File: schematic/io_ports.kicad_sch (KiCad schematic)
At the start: 5 parts, among them J1 Cartridge Port, J2 Expansion Port

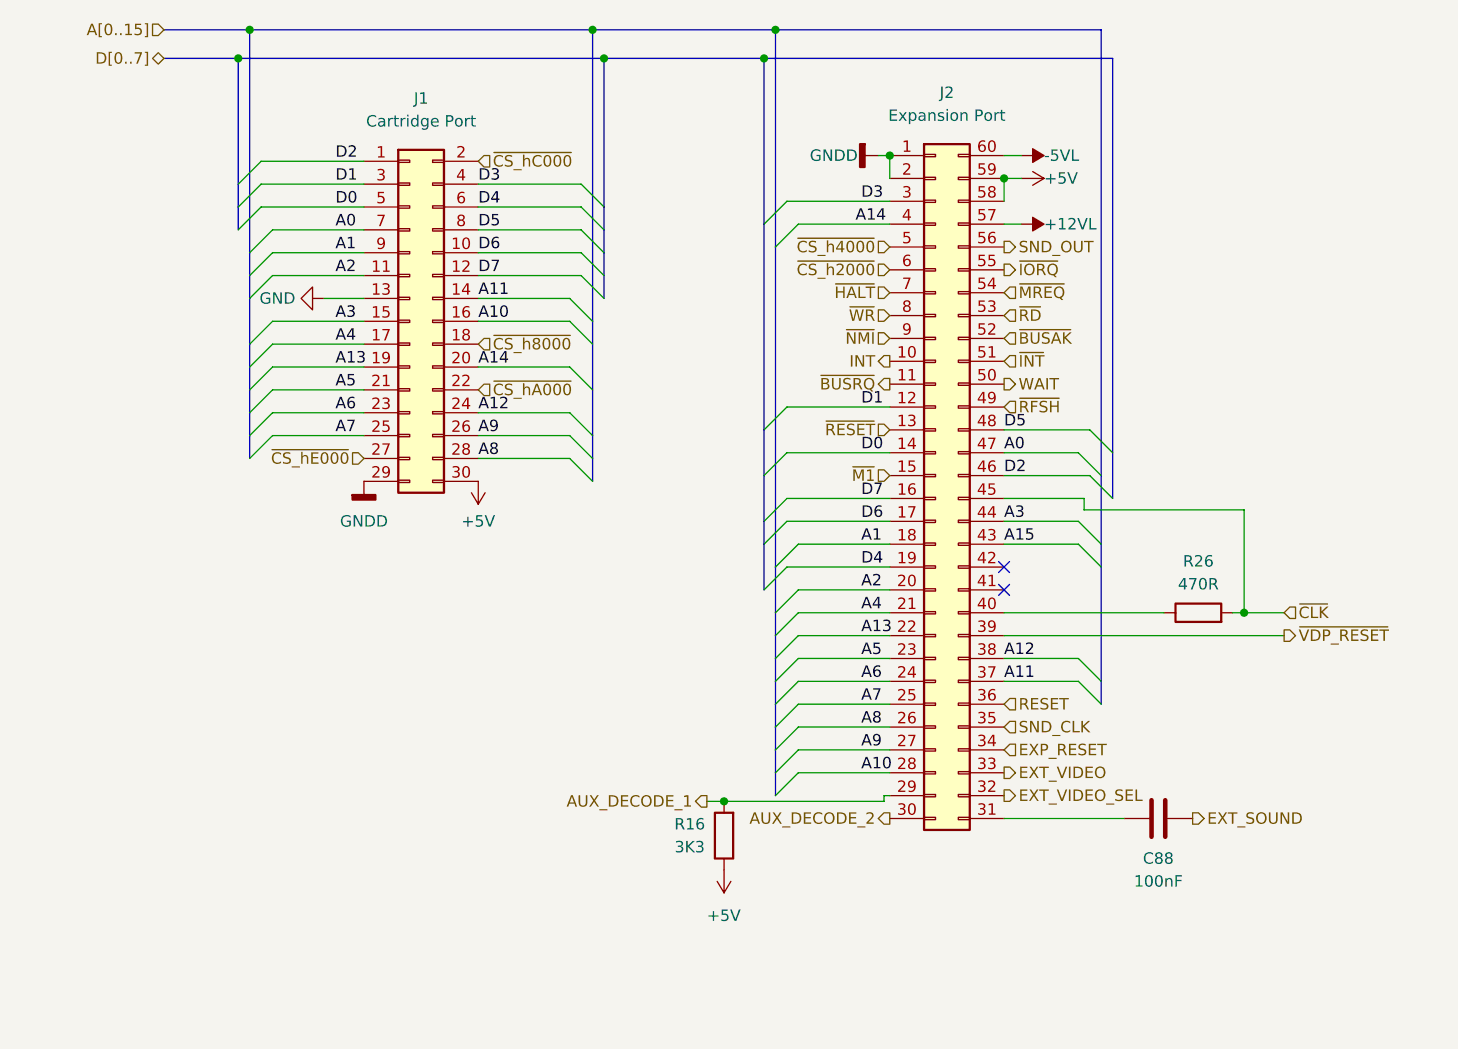
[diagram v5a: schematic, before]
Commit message: adjusted size of the sheets. added pcb version to the rev field. F.0... the 0 is for future fixes on my end. RF PCB is E.0.
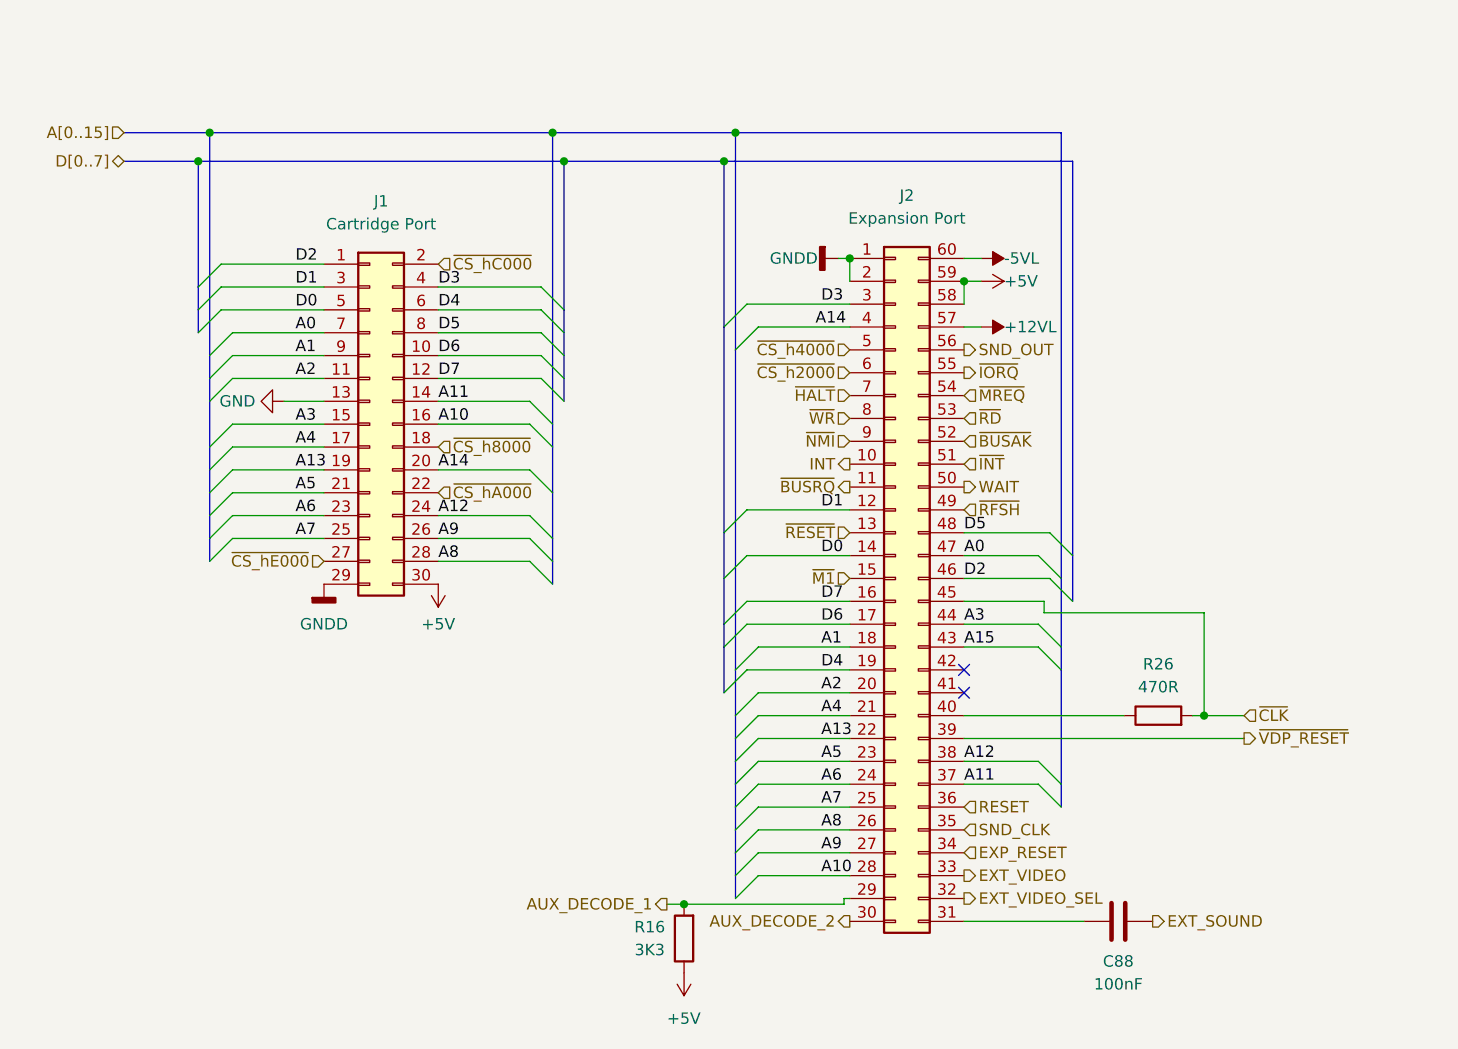
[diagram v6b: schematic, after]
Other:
- title: (none) -> Colecovision Schematic
- moved on the sheet: C88, J1, J2, R16, R26

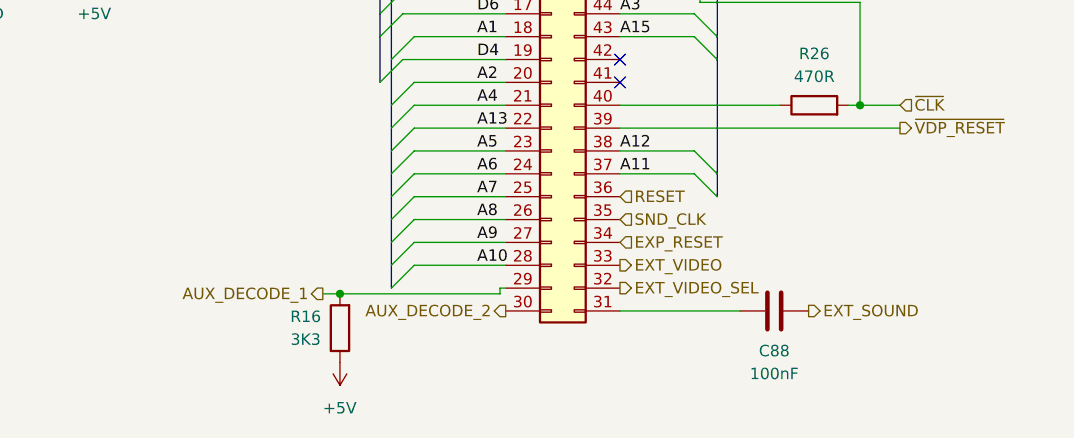
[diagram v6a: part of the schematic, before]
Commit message: cleanup, and started associating components
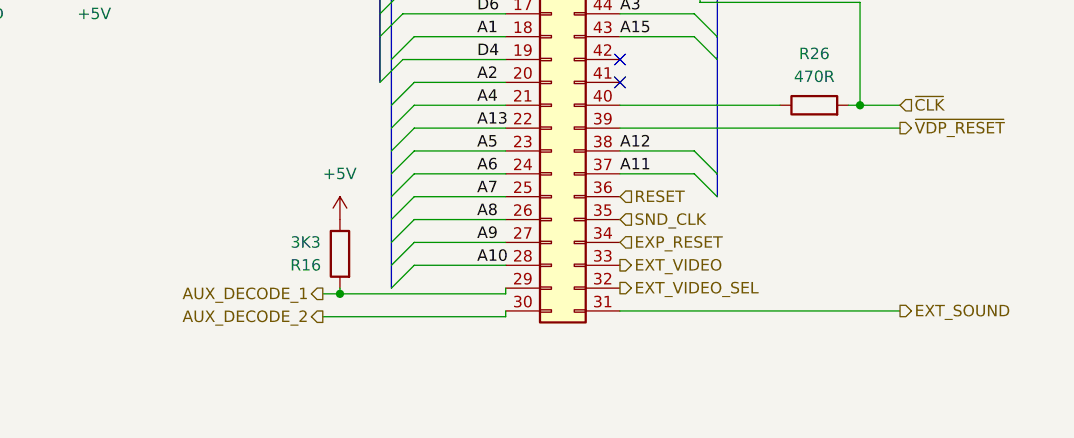
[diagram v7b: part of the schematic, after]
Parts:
- removed C88: 100nF, symbol Device:C
- R16, R26: footprint (none) -> Resistor_THT:R_Axial_DIN0207_L6.3mm_D2.5mm_P7.62mm_Horizontal
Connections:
- net EXT_SOUND: now also J2.31 (Pin_31)
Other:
- moved on the sheet: R16
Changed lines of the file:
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@@
+    (stroke (width 0) (type default) (color 0 0 0 0))
+  )
+  (wire (pts (xy 158.75 129.54) (xy 158.75 130.175))
     (stroke (width 0) (type default) (color 0 0 0 0))
   )
@@
     (stroke (width 0) (type default) (color 0 0 0 0))
   )
-  (wire (pts (xy 158.115 129.54) (xy 158.115 130.175))
-    (stroke (width 0) (type default) (color 0 0 0 0))
-  )
   (bus (pts (xy 125.73 44.45) (xy 125.73 76.835))
     (stroke (width 0) (type default) (color 0 0 0 0))
@@
     (stroke (width 0) (type default) (color 0 0 0 0))
   )
+  (wire (pts (xy 138.43 132.715) (xy 158.75 132.715))
+    (stroke (width 0) (type default) (color 0 0 0 0))
+  )
   (bus (pts (xy 144.78 101.6) (xy 144.78 106.68))
     (stroke (width 0) (type default) (color 0 0 0 0))
@@
     (stroke (width 0) (type default) (color 0 0 0 0))
   )
-  (wire (pts (xy 158.75 129.54) (xy 158.115 129.54))
-    (stroke (width 0) (type default) (color 0 0 0 0))
-  )
   (wire (pts (xy 171.45 109.22) (xy 189.23 109.22))
     (stroke (width 0) (type default) (color 0 0 0 0))
@@
     (stroke (width 0) (type default) (color 0 0 0 0))
   )
+  (wire (pts (xy 140.335 129.54) (xy 140.335 130.175))
+    (stroke (width 0) (type default) (color 0 0 0 0))
+  )
   (wire (pts (xy 180.34 97.79) (xy 198.12 97.79))
     (stroke (width 0) (type default) (color 0 0 0 0))
@@
     (stroke (width 0) (type default) (color 0 0 0 0))
   )
-  (wire (pts (xy 140.335 130.175) (xy 158.115 130.175))
+  (wire (pts (xy 140.335 130.175) (xy 158.75 130.175))
     (stroke (width 0) (type default) (color 0 0 0 0))
   )
@@
     (stroke (width 0) (type default) (color 0 0 0 0))
   )
-  (wire (pts (xy 171.45 132.08) (xy 184.785 132.08))
+  (wire (pts (xy 171.45 132.08) (xy 202.565 132.08))
     (stroke (width 0) (type default) (color 0 0 0 0))
   )
@@
     (stroke (width 0) (type default) (color 0 0 0 0))
   )
+  (wire (pts (xy 158.75 132.715) (xy 158.75 132.08))
+    (stroke (width 0) (type default) (color 0 0 0 0))
+  )
   (bus (pts (xy 127 69.215) (xy 127 71.755))
     (stroke (width 0) (type default) (color 0 0 0 0))
@@
     (effects (font (size 1.27 1.27)) (justify left bottom))
   )
-  (hierarchical_label "AUX_DECODE_2" (shape output) (at 158.75 132.08 180)
+  (hierarchical_label "AUX_DECODE_2" (shape output) (at 138.43 132.715 180)
     (effects (font (size 1.27 1.27)) (justify right))
   )
@@
     (effects (font (size 1.27 1.27)) (justify right))
   )
-  (hierarchical_label "EXT_SOUND" (shape output) (at 192.405 132.08 0)
+  (hierarchical_label "EXT_SOUND" (shape output) (at 202.565 132.08 0)
     (effects (font (size 1.27 1.27)) (justify left))
   )
@@
     (pin "9")
   )
-  (symbol (lib_id "power:+5V") (at 140.335 137.795 180) (unit 1)
+  (symbol (lib_id "power:+5V") (at 140.335 121.92 0) (mirror y) (unit 1)
     (in_bom yes) (on_board yes)
-    (property "Reference" "#PWR?" (id 0) (at 140.335 133.985 0)
-      (effects (font (size 1.27 1.27)) hide)
-    )
-    (property "Value" "+5V" (id 1) (at 138.43 142.875 0)
+    (property "Reference" "#PWR0201" (id 0) (at 140.335 125.73 0)
+      (effects (font (size 1.27 1.27)) hide)
+    )
+    (property "Value" "+5V" (id 1) (at 138.43 116.84 0)
       (effects (font (size 1.27 1.27)) (justify right))
     )
-    (property "Footprint" "" (id 2) (at 140.335 137.795 0)
-      (effects (font (size 1.27 1.27)) hide)
-    )
-    (property "Datasheet" "" (id 3) (at 140.335 137.795 0)
+    (property "Footprint" "" (id 2) (at 140.335 121.92 0)
+      (effects (font (size 1.27 1.27)) hide)
+    )
+    (property "Datasheet" "" (id 3) (at 140.335 121.92 0)
       (effects (font (size 1.27 1.27)) hide)
     )
@@
     (property "Reference" "R26" (id 0) (at 193.04 103.505 90))
     (property "Value" "470R" (id 1) (at 193.04 106.045 90))
-    (property "Footprint" "" (id 2) (at 193.04 110.998 90)
+    (property "Footprint" "Resistor_THT:R_Axial_DIN0207_L6.3mm_D2.5mm_P7.62mm_Horizontal" (id 2) (at 193.04 110.998 90)
       (effects (font (size 1.27 1.27)) hide)
     )
@@
   (symbol (lib_id "power:+5V") (at 173.355 60.96 270) (unit 1)
     (in_bom yes) (on_board yes)
-    (property "Reference" "#PWR?" (id 0) (at 169.545 60.96 0)
+    (property "Reference" "#PWR0204" (id 0) (at 169.545 60.96 0)
       (effects (font (size 1.27 1.27)) hide)
     )
@@
     (pin "9")
   )
-  (symbol (lib_id "Device:R") (at 140.335 133.985 180) (unit 1)
+  (symbol (lib_id "Device:R") (at 140.335 125.73 0) (mirror y) (unit 1)
     (in_bom yes) (on_board yes)
-    (property "Reference" "R16" (id 0) (at 136.525 132.715 0))
-    (property "Value" "3K3" (id 1) (at 136.525 135.255 0))
-    (property "Footprint" "" (id 2) (at 142.113 133.985 90)
-      (effects (font (size 1.27 1.27)) hide)
-    )
-    (property "Datasheet" "~" (id 3) (at 140.335 133.985 0)
+    (property "Reference" "R16" (id 0) (at 136.525 127 0))
+    (property "Value" "3K3" (id 1) (at 136.525 124.46 0))
+    (property "Footprint" "Resistor_THT:R_Axial_DIN0207_L6.3mm_D2.5mm_P7.62mm_Horizontal" (id 2) (at 142.113 125.73 90)
+      (effects (font (size 1.27 1.27)) hide)
+    )
+    (property "Datasheet" "~" (id 3) (at 140.335 125.73 0)
       (effects (font (size 1.27 1.27)) hide)
     )
@@
   (symbol (lib_id "Power_Symbols:-5VL") (at 173.355 58.42 270) (unit 1)
     (in_bom yes) (on_board yes)
-    (property "Reference" "#PWR?" (id 0) (at 175.895 58.42 0)
+    (property "Reference" "#PWR0203" (id 0) (at 175.895 58.42 0)
       (effects (font (size 1.27 1.27)) hide)
     )
@@
   (symbol (lib_id "power:+5V") (at 113.03 94.615 180) (unit 1)
     (in_bom yes) (on_board yes) (fields_autoplaced)
-    (property "Reference" "#PWR?" (id 0) (at 113.03 90.805 0)
+    (property "Reference" "#PWR0200" (id 0) (at 113.03 90.805 0)
       (effects (font (size 1.27 1.27)) hide)
     )
@@
   (symbol (lib_id "power:GNDD") (at 157.48 58.42 270) (unit 1)
     (in_bom yes) (on_board yes)
-    (property "Reference" "#PWR?" (id 0) (at 151.13 58.42 0)
+    (property "Reference" "#PWR0202" (id 0) (at 151.13 58.42 0)
       (effects (font (size 1.27 1.27)) hide)
     )
@@
     (pin "1")
   )
-  (symbol (lib_id "Device:C") (at 188.595 132.08 90) (unit 1)
-    (in_bom yes) (on_board yes)
-    (property "Reference" "C88" (id 0) (at 188.595 136.525 90))
-    (property "Value" "100nF" (id 1) (at 188.595 139.065 90))
-    (property "Footprint" "" (id 2) (at 192.405 131.1148 0)
-      (effects (font (size 1.27 1.27)) hide)
-    )
-    (property "Datasheet" "~" (id 3) (at 188.595 132.08 0)
-      (effects (font (size 1.27 1.27)) hide)
-    )
-    (pin "1")
-    (pin "2")
-  )
   (symbol (lib_id "Power_Symbols:+12VL") (at 173.355 66.04 270) (unit 1)
     (in_bom yes) (on_board yes)
-    (property "Reference" "#PWR?" (id 0) (at 175.895 66.04 0)
+    (property "Reference" "#PWR0205" (id 0) (at 175.895 66.04 0)
       (effects (font (size 1.27 1.27)) hide)
     )
@@
   (symbol (lib_id "power:GND") (at 95.885 74.295 270) (unit 1)
     (in_bom yes) (on_board yes)
-    (property "Reference" "#PWR?" (id 0) (at 89.535 74.295 0)
+    (property "Reference" "#PWR0198" (id 0) (at 89.535 74.295 0)
       (effects (font (size 1.27 1.27)) hide)
     )
@@
   (symbol (lib_id "power:GNDD") (at 100.33 94.615 0) (unit 1)
     (in_bom yes) (on_board yes) (fields_autoplaced)
-    (property "Reference" "#PWR?" (id 0) (at 100.33 100.965 0)
-      (effects (font (size 1.27 1.27)) hide)
-    )
+    (property "Reference" "#PWR0199" (id 0) (at 100.33 100.965 0)
+      (effects (font (size 1.27 1.27)) hide)
+    )

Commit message: added new libs for rest of the parts. some still need updating for correct parts, but for now they work. PCB import complete.
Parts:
- J1: footprint (none) -> TE_5530841-2:55308412
- J2: footprint (none) -> Connector_PCBEdge_EXT:Colecovision_Expansion
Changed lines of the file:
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@@
     (property "Reference" "J1" (id 0) (at 106.68 52.07 0))
     (property "Value" "Cartridge Port" (id 1) (at 106.68 54.61 0))
-    (property "Footprint" "" (id 2) (at 105.41 76.835 0)
+    (property "Footprint" "TE_5530841-2:55308412" (id 2) (at 105.41 76.835 0)
       (effects (font (size 1.27 1.27)) hide)
     )
@@
     (property "Reference" "J2" (id 0) (at 165.1 51.435 0))
     (property "Value" "Expansion Port" (id 1) (at 165.1 53.975 0))
-    (property "Footprint" "" (id 2) (at 163.83 93.98 0)
+    (property "Footprint" "Connector_PCBEdge_EXT:Colecovision_Expansion" (id 2) (at 163.83 93.98 0)
       (effects (font (size 1.27 1.27)) hide)
     )
